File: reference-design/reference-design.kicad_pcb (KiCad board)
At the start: 2 copper layers, 104 x 83.9 mm, 21 parts

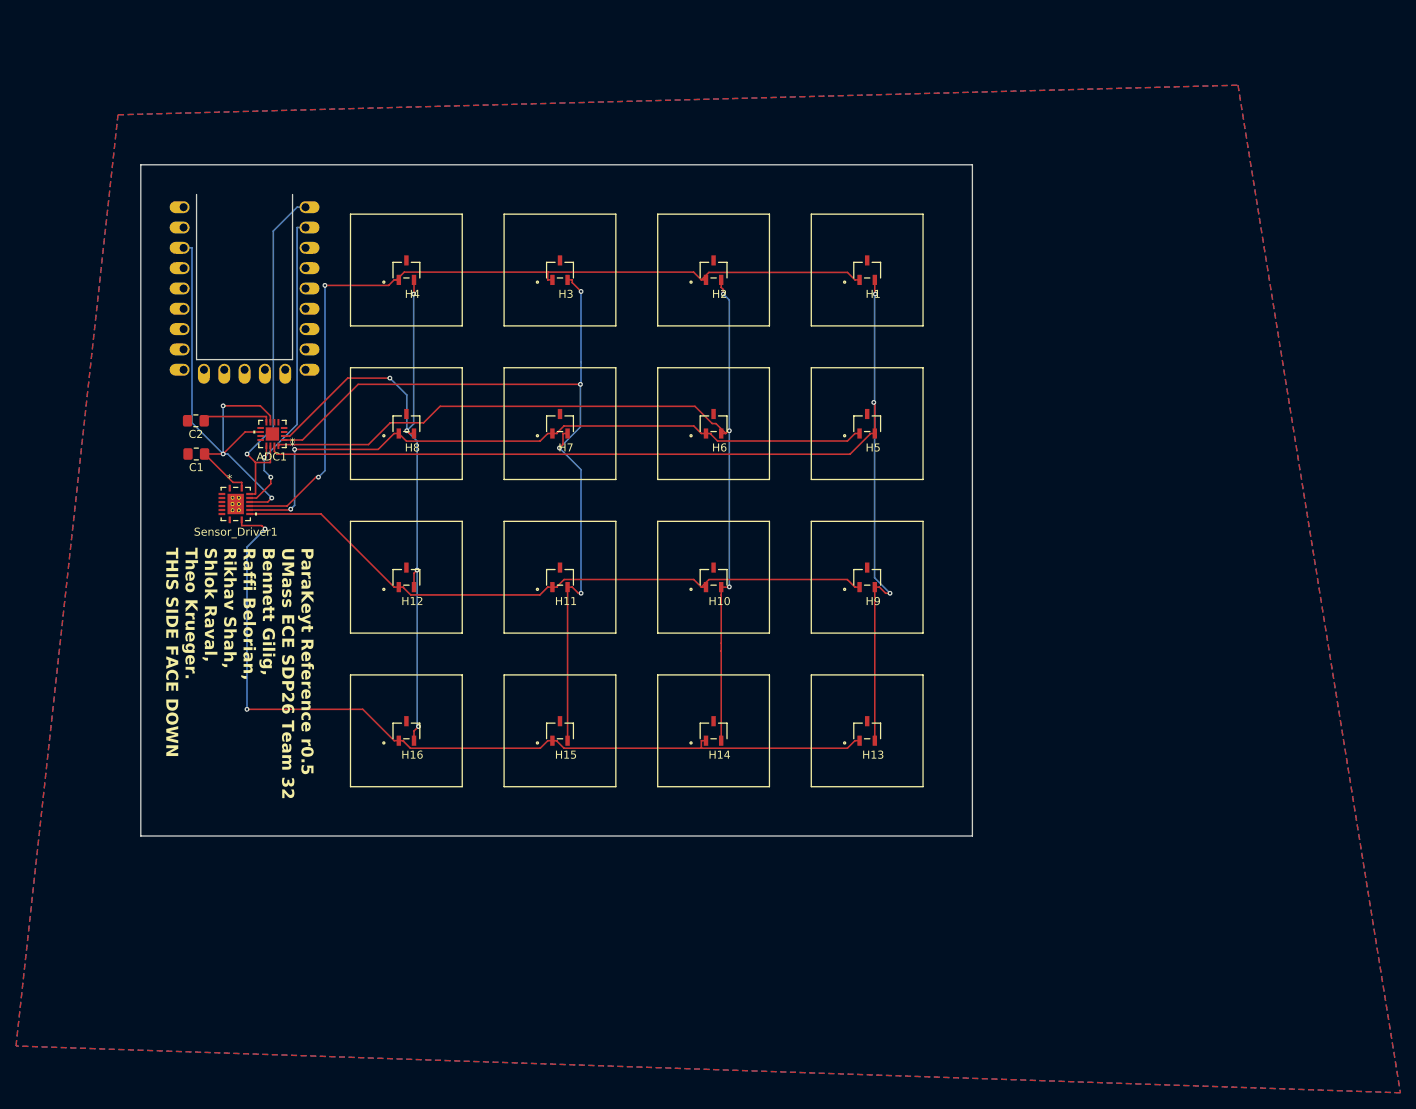
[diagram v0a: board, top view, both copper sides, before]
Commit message: fix unconnected and ground plane interference problems. AAAAAAAA
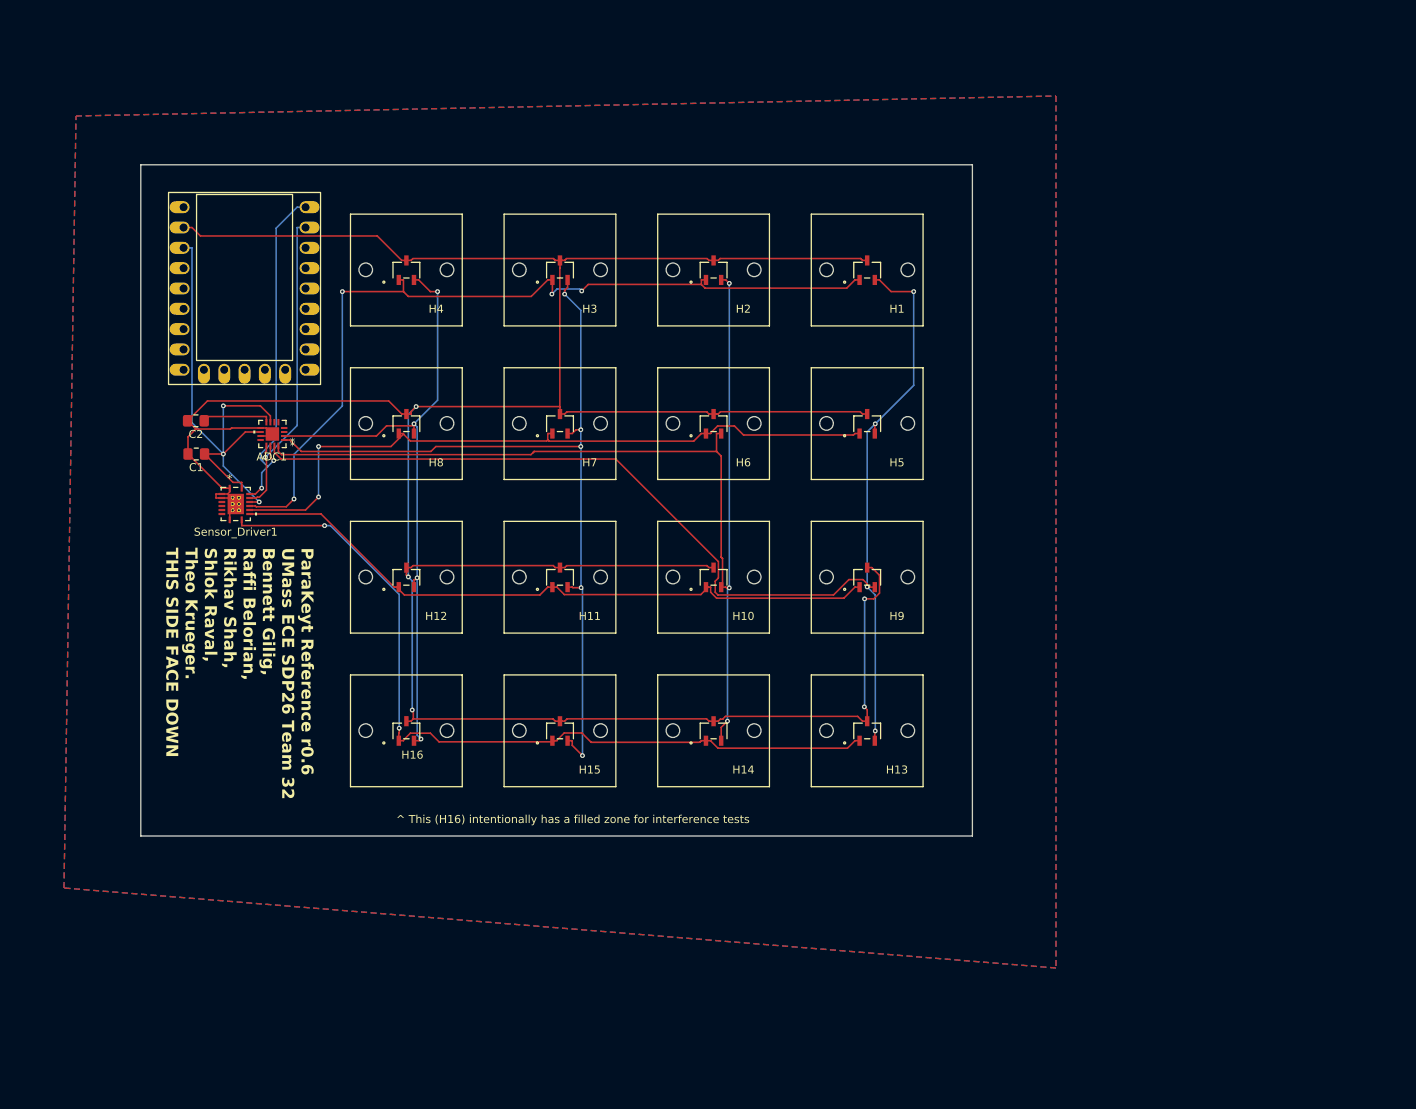
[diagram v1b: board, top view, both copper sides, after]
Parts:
- H16: footprint AH49FNTR_G1:SC59_DIO_KeyswitchOutline -> AH49FNTR_G1:SC59_DIO_KeyswitchOutline_NoRuleArea
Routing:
- net GND: track 0.00 -> 388.4 mm, vias 0 -> 5
- net col1: track 119.6 -> 136.3 mm
- net col0: track 142.5 -> 153.2 mm, vias 3 -> 4
- net row3: track 108.7 -> 102.9 mm
- net col3: track 85.8 -> 81.4 mm, vias 5 -> 4
- net +3.3V: track 68.0 -> 65.7 mm
- net col2: track 106.2 -> 105.0 mm, vias 4 -> 5
- net row1: track 86.7 -> 87.8 mm
- net row0: track 105.5 -> 106.6 mm, vias 2 -> 4
- net i2c0_sda: track 44.6 -> 43.6 mm, vias 1 -> 2
- net row2: track 83.1 -> 83.7 mm
- net i2c0_scl: track 40.1 -> 39.6 mm, vias 2 -> 1
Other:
- board text added: "ParaKeyt Reference r0.6 UMass ECE SDP26 Team 32 Bennett Gilig, Raffi Belorian, Rikhav Shah, Shlok Raval, Theo Krueger. THIS SIDE FACE DOWN"
- board text added: "^ This (H16) intentionally has a filled zone for interference tests"
- board text removed: "ParaKeyt Reference r0.5 UMass ECE SDP26 Team 32 Bennett Gilig, Raffi Belorian, Rikhav Shah, Shlok Raval, Theo Krueger. THIS SIDE FACE DOWN"

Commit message: add testpoints
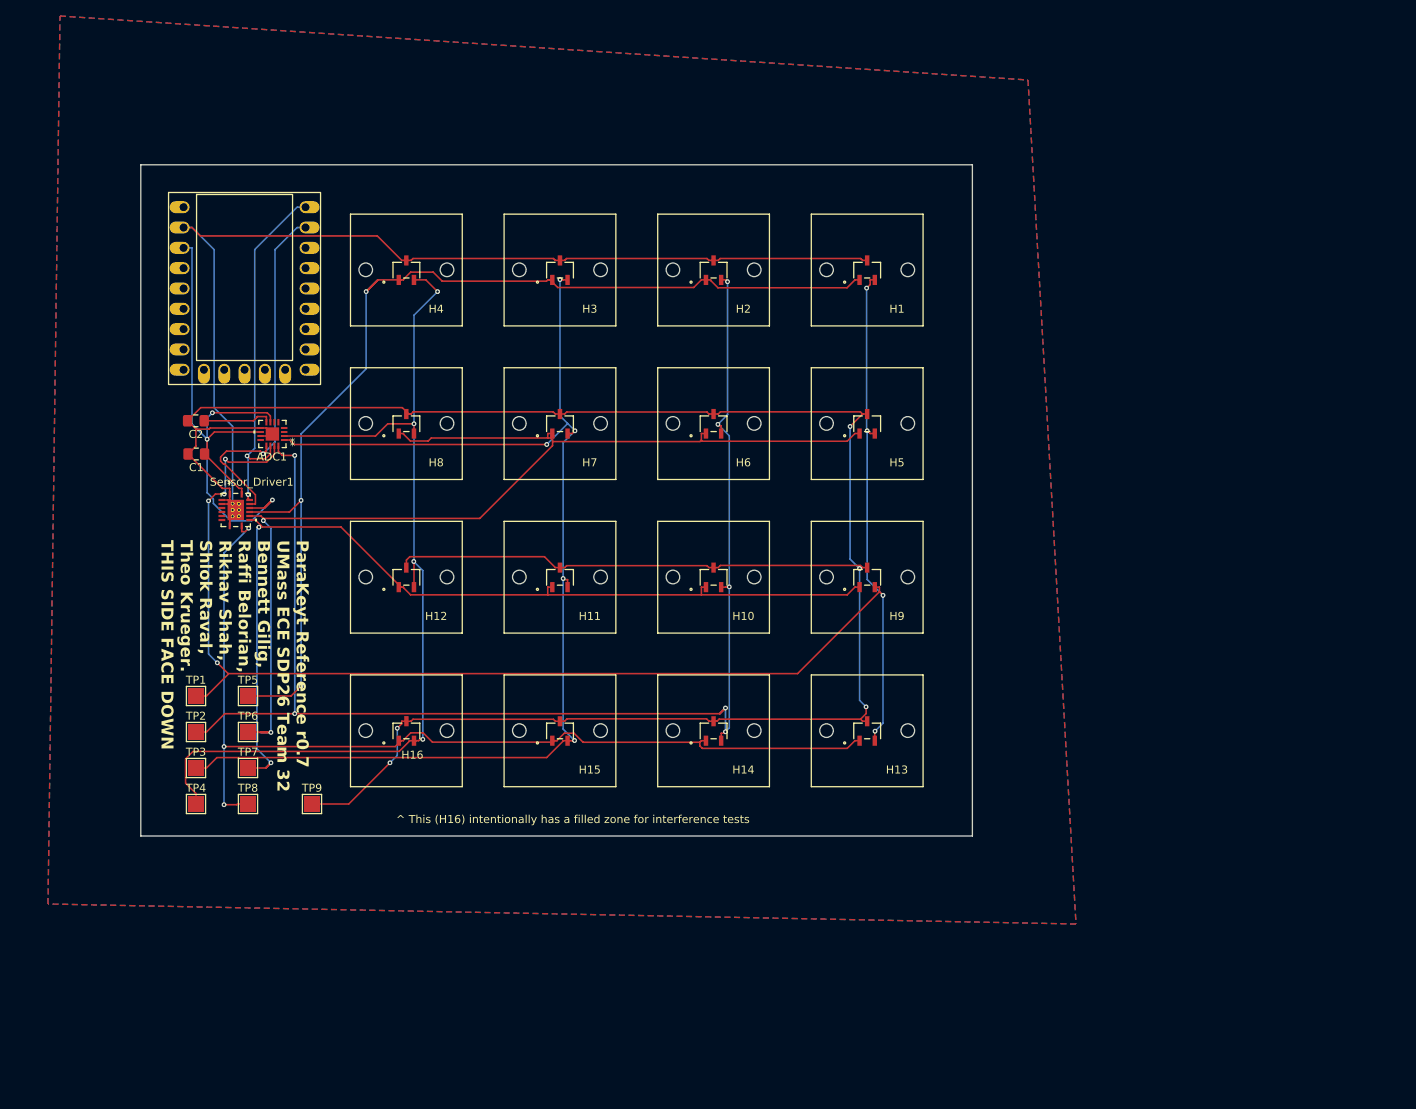
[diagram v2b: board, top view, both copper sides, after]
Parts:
- added TP1: col0, TestPoint:TestPoint_Pad_2.0x2.0mm, F.Cu at (19.0, 78.5)
- added TP2: col1, TestPoint:TestPoint_Pad_2.0x2.0mm, F.Cu at (19.0, 83.0)
- added TP3: col2, TestPoint:TestPoint_Pad_2.0x2.0mm, F.Cu at (19.0, 87.5)
- added TP4: col3, TestPoint:TestPoint_Pad_2.0x2.0mm, F.Cu at (19.0, 92.0)
- added TP5: row0, TestPoint:TestPoint_Pad_2.0x2.0mm, F.Cu at (25.5, 78.5)
- added TP6: row1, TestPoint:TestPoint_Pad_2.0x2.0mm, F.Cu at (25.5, 83.0)
- added TP7: row2, TestPoint:TestPoint_Pad_2.0x2.0mm, F.Cu at (25.5, 87.5)
- added TP8: row3, TestPoint:TestPoint_Pad_2.0x2.0mm, F.Cu at (25.5, 92.0)
- added TP9: GND, TestPoint:TestPoint_Pad_2.0x2.0mm, F.Cu at (33.5, 92.0)
- moved Sensor_Driver1 0.75 mm to (24.0, 55.2)
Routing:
- net row1: track 87.8 -> 139.5 mm
- net col2: track 105.0 -> 148.7 mm
- net row2: track 83.7 -> 122.4 mm, vias 0 -> 2
- net col3: track 81.4 -> 119.4 mm
- net col0: track 153.2 -> 190.5 mm, vias 4 -> 8
- net col1: track 136.3 -> 172.1 mm, vias 3 -> 7
- net row0: track 106.6 -> 140.3 mm, vias 4 -> 3
- net GND: track 388.4 -> 422.0 mm
- net row3: track 102.9 -> 124.7 mm, vias 2 -> 3
- net +3.3V: track 65.7 -> 80.3 mm
- net i2c0_scl: track 39.6 -> 46.6 mm
- net i2c0_sda: track 43.6 -> 44.8 mm
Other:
- board text added: "ParaKeyt Reference r0.7 UMass ECE SDP26 Team 32 Bennett Gilig, Raffi Belorian, Rikhav Shah, Shlok Raval, Theo Krueger. THIS SIDE FACE DOWN"
- board text removed: "ParaKeyt Reference r0.6 UMass ECE SDP26 Team 32 Bennett Gilig, Raffi Belorian, Rikhav Shah, Shlok Raval, Theo Krueger. THIS SIDE FACE DOWN"
